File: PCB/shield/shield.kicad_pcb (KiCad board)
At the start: 2 copper layers, 70.5 x 87.7 mm, 17 parts, among them J1 QTR-8A, J13 Motor, J3 Servo, J4 Battery, Q1 SI2301DS, SW1 SW_SPST, U1 WeAct-ESP32-S3-A, U3 TB6612FNG, U4 MP1584EN

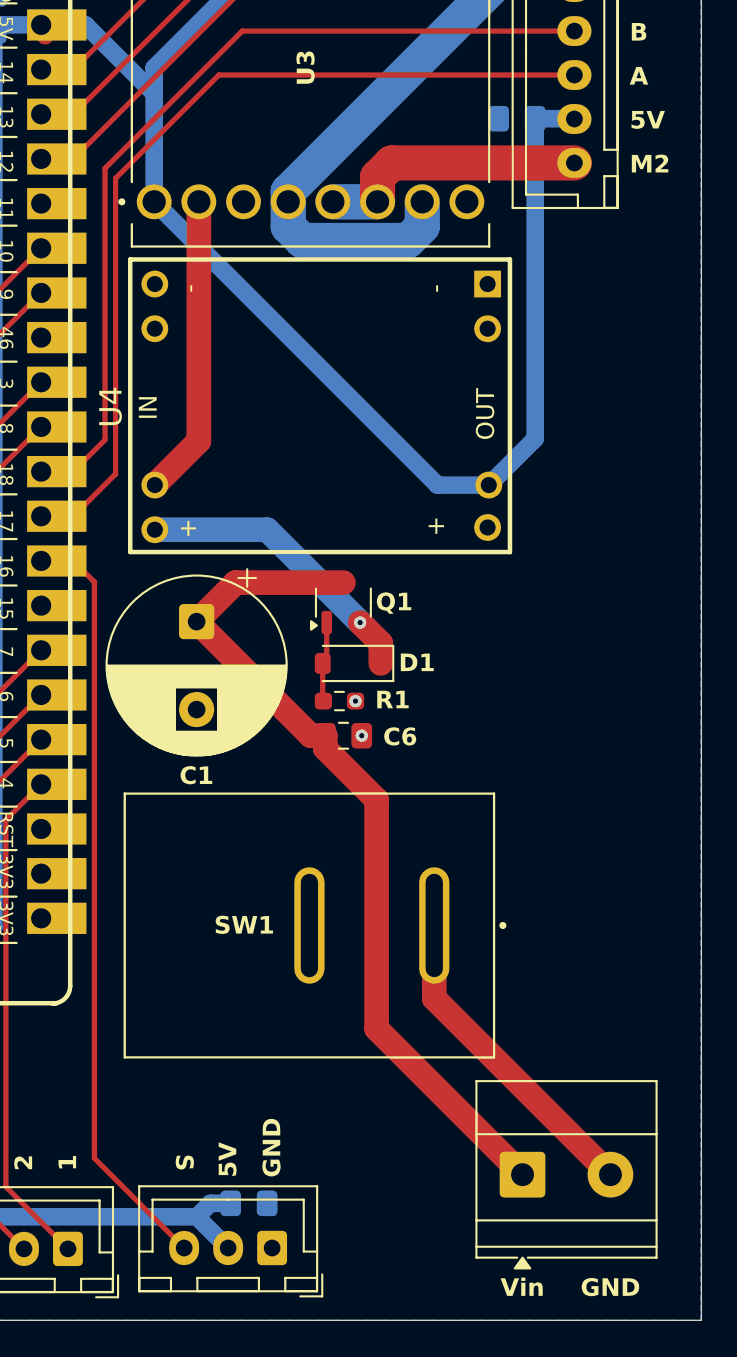
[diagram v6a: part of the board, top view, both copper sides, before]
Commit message: feat: rearrange pcb footprints; change mosfet
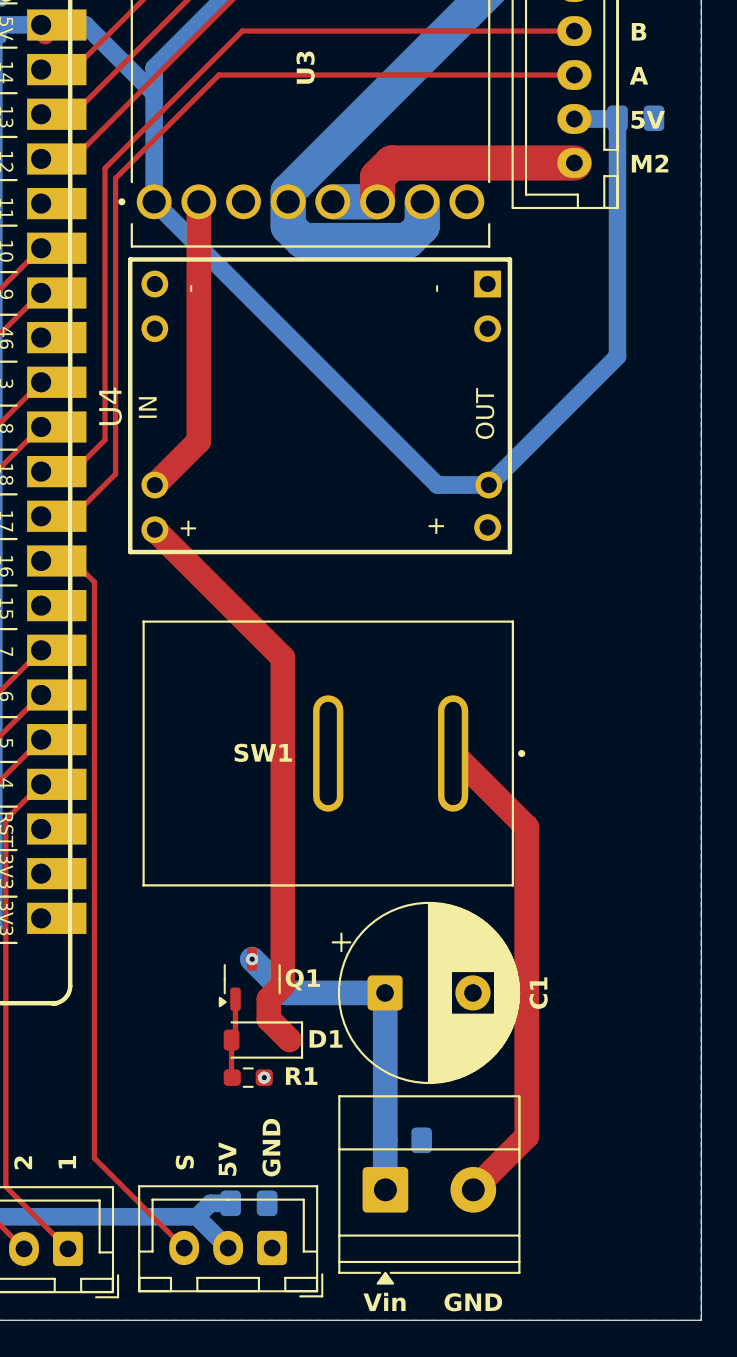
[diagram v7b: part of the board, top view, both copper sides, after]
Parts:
- C6: moved to B.Cu
- Q1: value SI2301DS -> IRLML6402TRPBF
- moved C1 23.7 mm to (149.0, 106.7), turned to 0 degrees
- moved C6 23.3 mm to (150.1, 115.1)
- moved Q1 22.0 mm to (141.5, 105.9)
- moved D1 22.0 mm to (141.9, 109.4)
- moved R1 22.0 mm to (141.2, 111.5)
- moved SW1 9.84 mm to (145.8, 93.1)
- moved J4 7.85 mm to (149.0, 117.9)
- moved C7 6.76 mm to (163.3, 56.9), turned to 0 degrees
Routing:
- net Net-(J4-Pin_1): track 48.9 -> 19.6 mm, vias 0 -> 1
- net VCC: track 33.8 -> 50.0 mm, vias 1 -> 0
- net Net-(J4-Pin_2): track 18.3 -> 27.8 mm
- net +5V: track 191.3 -> 193.5 mm
- net GND: vias 2 -> 1

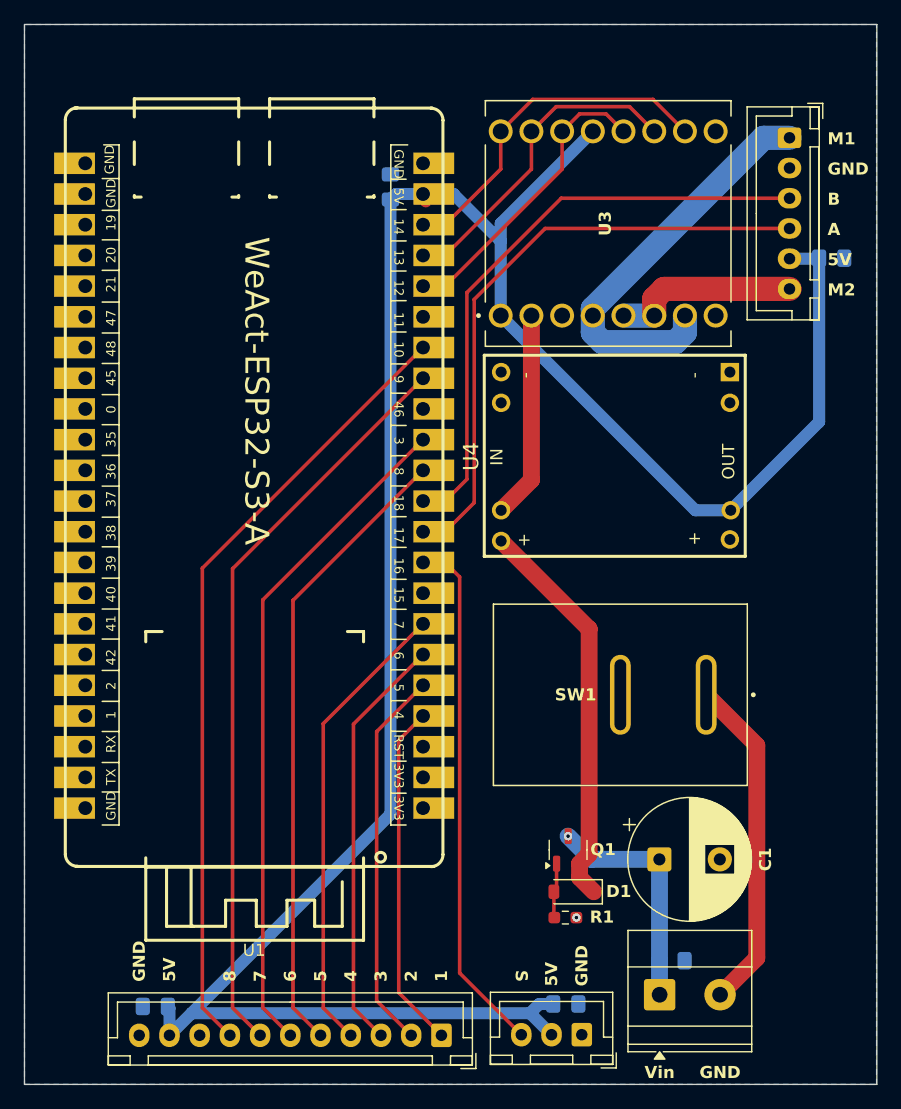
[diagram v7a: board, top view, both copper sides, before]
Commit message: minor: add measurement in pcb drawing
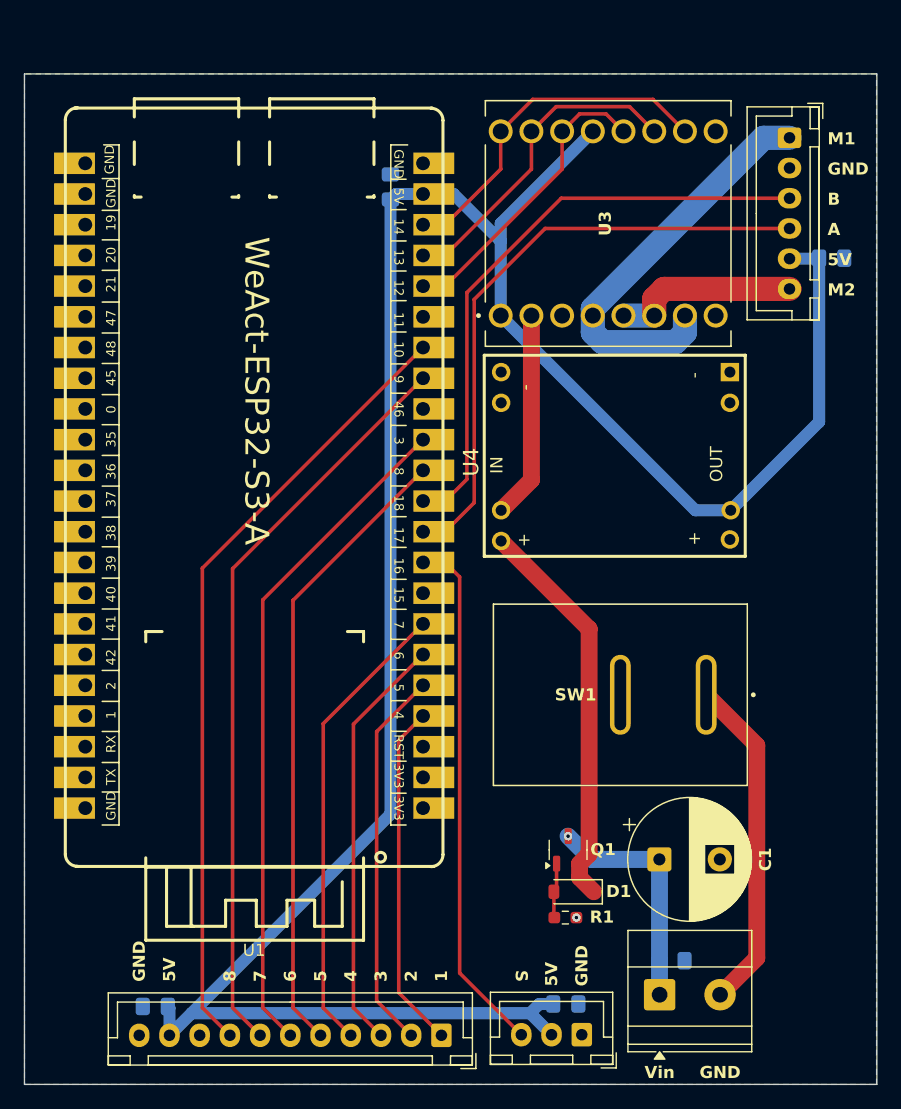
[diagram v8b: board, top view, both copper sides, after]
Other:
- board size 70.5 x 87.7 mm -> 70.5 x 83.6 mm
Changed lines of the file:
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@@
 		(descr "MP1584EN Adjustable Buck Converter 12V-24V to 5V 3A")
 		(property "Reference" "U4"
-			(at 8.257 -1.085 90)
+			(at 7.8 -1.085 90)
 			(layer "F.SilkS")
 			(effects
@@
 		)
 		(property "Value" "MP1584EN"
-			(at 8.257 22.552 90)
+			(at 8.257 21.552 90)
 			(layer "F.Fab")
 			(effects
@@
 		)
 		(fp_text user "-"
-			(at 14.732 2.794 90)
+			(at 13.732 2.794 90)
 			(unlocked yes)
 			(layer "F.SilkS")
@@
 		)
 		(fp_text user "IN"
-			(at 7.493 0.4394 90)
+			(at 6.822705 0.4394 90)
 			(unlocked yes)
 			(layer "F.SilkS")
@@
 		)
 		(fp_text user "OUT"
-			(at 6.35 19.6164 90)
+			(at 6.145372 18.6164 90)
 			(unlocked yes)
 			(layer "F.SilkS")
@@
 		)
 	)
+	(gr_line
+		(start 172.974 34.5948)
+		(end 182.974 34.5948)
+		(stroke
+			(width 0.1)
+			(type solid)
+		)
+		(layer "Dwgs.User")
+	)
 	(gr_rect
-		(start 96.4946 37.61452)
+		(start 96.4946 41.70392)
 		(end 167.005 125.29532)
 		(stroke
@@
 		)
 	)
+	(dimension
+		(type aligned)
+		(layer "Dwgs.User")
+		(pts
+			(xy 172.974 34.5948) (xy 182.974 34.5948)
+		)
+		(height -3.1496)
+		(format
+			(prefix "")
+			(suffix "")
+			(units 3)
+			(units_format 0)
+			(precision 4)
+			(suppress_zeroes yes)
+		)
+		(style
+			(thickness 0.1)
+			(arrow_length 1.27)
+			(text_position_mode 0)
+			(arrow_direction outward)
+			(extension_height 0.58642)
+			(extension_offset 0.5)
+			(keep_text_aligned yes)
+		)
+		(gr_text "10"
+			(at 177.974 30.2952 0)
+			(layer "Dwgs.User")
+			(effects
+				(font
+					(size 1 1)
+					(thickness 0.15)
+				)
+			)
+		)
+	)
+	(dimension
+		(type aligned)
+		(layer "Dwgs.User")
+		(pts
+			(xy 96.4946 41.7068) (xy 96.4692 125.3236)
+		)
+		(height 17.78)
+		(format
+			(prefix "")
+			(suffix "")
+			(units 3)
+			(units_format 0)
+			(precision 4)
+			(suppress_zeroes yes)
+		)
+		(style
+			(thickness 0.1)
+			(arrow_length 1.27)
+			(text_position_mode 0)
+			(arrow_direction outward)
+			(extension_height 0.58642)
+			(extension_offset 0.5)
+			(keep_text_aligned yes)
+		)
+		(gr_text "83.6168"
+			(at 77.551901 83.50945 89.98259545)
+			(layer "Dwgs.User")
+			(effects
+				(font
+					(size 1 1)
+					(thickness 0.15)
+				)
+			)
+		)
+	)
+	(dimension
+		(type aligned)
+		(layer "Dwgs.User")
+		(pts
+			(xy 96.4946 41.7068) (xy 167.005 41.7068)
+		)
+		(height -10.8712)
+		(format
+			(prefix "")
+			(suffix "")
+			(units 3)
+			(units_format 0)
+			(precision 4)
+			(suppress_zeroes yes)
+		)
+		(style
+			(thickness 0.1)
+			(arrow_length 1.27)
+			(text_position_mode 0)
+			(arrow_direction outward)
+			(extension_height 0.58642)
+			(extension_offset 0.5)
+			(keep_text_aligned yes)
+		)
+		(gr_text "70.5104"
+			(at 131.7498 29.6856 0)
+			(layer "Dwgs.User")
+			(effects
+				(font
+					(size 1 1)
+					(thickness 0.15)
+				)
+			)
+		)
+	)
 	(segment
 		(start 143.2052 106.2432)
@@
 	)
 	(segment
-		(start 129.56246 52.1169)
-		(end 129.69608 52.25052)
-		(width 1)
-		(layer "F.Cu")
-		(net 20)
-	)
-	(segment
 		(start 108.4872 118.9813)
 		(end 108.3525 118.8466)
@@
 		(polygon
 			(pts
-				(xy 166.9796 125.2982) (xy 166.9796 37.6174) (xy 96.4946 37.6174) (xy 96.4946 125.2982)
+				(xy 166.9796 125.2982) (xy 166.9796 41.7068) (xy 96.4946 41.7068) (xy 96.4946 125.2982)
 			)
 		)
